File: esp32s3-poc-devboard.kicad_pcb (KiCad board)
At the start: 4 copper layers, 97 parts, among them J1 24VDC, J2 Conn_01x01_Pin, J3 USB_C_Receptacle_USB2.0_14P, J4 USB_C_Receptacle_USB2.0_14P, J5 Screw_Terminal_01x06, J6 Conn_Coaxial, J7 Conn_01x16_Pin, J8 Screw_Terminal_01x04, Q3 MMDT5551, SW1 SW_Push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

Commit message: add 24V symbol and netclass
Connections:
- net Net-(J1-Pin_2) renamed +24V
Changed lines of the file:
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@@
 	(net 3 "+5V")
 	(net 4 "Net-(JP2-A)")
-	(net 5 "Net-(J1-Pin_2)")
+	(net 5 "+24V")
 	(net 6 "Net-(U4-BOOT)")
 	(net 7 "Net-(D3-K)")
@@
 			(layers "*.Cu" "*.Mask")
 			(remove_unused_layers no)
-			(net 5 "Net-(J1-Pin_2)")
+			(net 5 "+24V")
 			(pinfunction "Pin_2")
 			(pintype "passive")
@@
 			(size 1.55 0.6)
 			(layers "F.Cu" "F.Mask" "F.Paste")
-			(net 5 "Net-(J1-Pin_2)")
+			(net 5 "+24V")
 			(pinfunction "VIN")
 			(pintype "power_in")
@@
 			(layers "F.Cu" "F.Mask" "F.Paste")
 			(roundrect_rratio 0.25)
-			(net 5 "Net-(J1-Pin_2)")
+			(net 5 "+24V")
 			(pintype "passive")
 		)

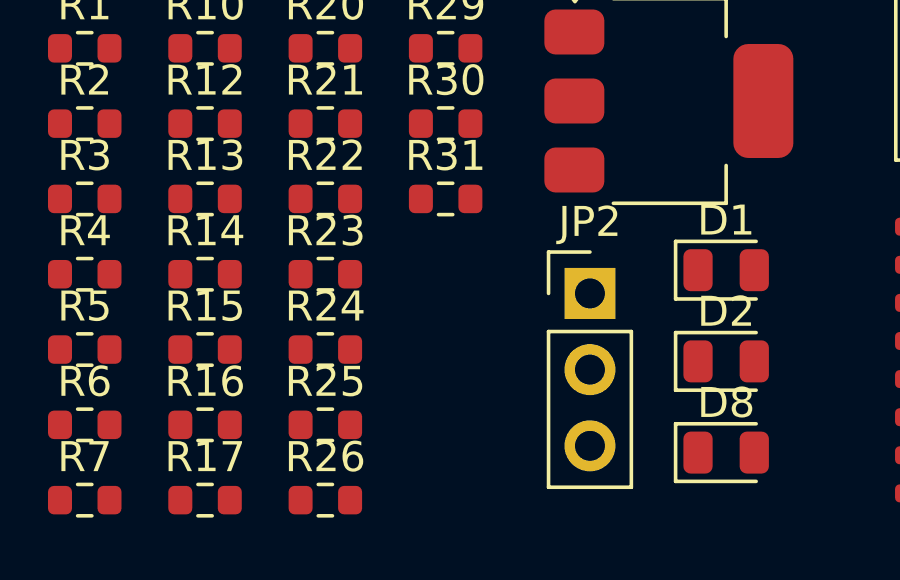
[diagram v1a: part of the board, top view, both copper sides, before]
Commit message: add missing R11 footprint
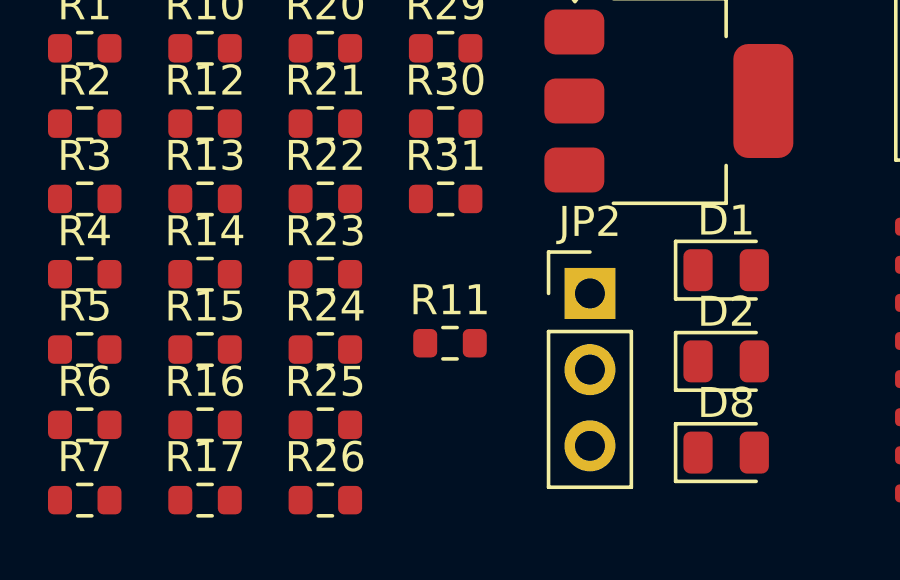
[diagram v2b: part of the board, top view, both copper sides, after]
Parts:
- added R11: R, Resistor_SMD:R_0603_1608Metric, F.Cu at (65.3, 179.5)
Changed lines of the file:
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@@
+		)
+	)
+	(footprint "Resistor_SMD:R_0603_1608Metric"
+		(layer "F.Cu")
+		(at 65.325 179.5)
+		(descr "Resistor SMD 0603 (1608 Metric), square (rectangular) end terminal, IPC-7351 nominal, (Body size source: IPC-SM-782 page 72, https://www.pcb-3d.com/wordpress/wp-content/uploads/ipc-sm-782a_amendment_1_and_2.pdf), generated with kicad-footprint-generator")
+		(tags "resistor")
+		(property "Reference" "R11"
+			(at 0 -1.43 0)
+			(layer "F.SilkS")
+			(effects
+				(font
+					(size 1 1)
+					(thickness 0.15)
+				)
+			)
+		)
+		(property "Value" "R"
+			(at 0 1.43 0)
+			(layer "F.Fab")
+			(effects
+				(font
+					(size 1 1)
+					(thickness 0.15)
+				)
+			)
+		)
+		(property "Datasheet" "~"
+			(at 0 0 0)
+			(layer "F.Fab")
+			(hide yes)
+			(effects
+				(font
+					(size 1.27 1.27)
+					(thickness 0.15)
+				)
+			)
+		)
+		(property "Description" "Resistor"
+			(at 0 0 0)
+			(layer "F.Fab")
+			(hide yes)
+			(effects
+				(font
+					(size 1.27 1.27)
+					(thickness 0.15)
+				)
+			)
+		)
+		(property "JLCPCB Part Number" ""
+			(at 0 0 0)
+			(unlocked yes)
+			(layer "F.Fab")
+			(hide yes)
+			(effects
+				(font
+					(size 1 1)
+					(thickness 0.15)
+				)
+			)
+		)
+		(property "Manufacturer" ""
+			(at 0 0 0)
+			(unlocked yes)
+			(layer "F.Fab")
+			(hide yes)
+			(effects
+				(font
+					(size 1 1)
+					(thickness 0.15)
+				)
+			)
+		)
+		(property "Manufacturer Part Number" ""
+			(at 0 0 0)
+			(unlocked yes)
+			(layer "F.Fab")
+			(hide yes)
+			(effects
+				(font
+					(size 1 1)
+					(thickness 0.15)
+				)
+			)
+		)
+		(property "Basic" ""
+			(at 0 0 0)
+			(unlocked yes)
+			(layer "F.Fab")
+			(hide yes)
+			(effects
+				(font
+					(size 1 1)
+					(thickness 0.15)
+				)
+			)
+		)
+		(property ki_fp_filters "R_*")
+		(sheetname "/")
+		(sheetfile "esp32s3-poc-devboard.kicad_sch")
+		(attr smd dnp)
+		(fp_line
+			(start -0.237258 -0.5225)
+			(end 0.237258 -0.5225)
+			(stroke
+				(width 0.12)
+				(type solid)
+			)
+			(layer "F.SilkS")
+		)
+		(fp_line
+			(start -0.237258 0.5225)
+			(end 0.237258 0.5225)
+			(stroke
+				(width 0.12)
+				(type solid)
+			)
+			(layer "F.SilkS")
+		)
+		(fp_line
+			(start -1.48 -0.73)
+			(end 1.48 -0.73)
+			(stroke
+				(width 0.05)
+				(type solid)
+			)
+			(layer "F.CrtYd")
+		)
+		(fp_line
+			(start -1.48 0.73)
+			(end -1.48 -0.73)
+			(stroke
+				(width 0.05)
+				(type solid)
+			)
+			(layer "F.CrtYd")
+		)
+		(fp_line
+			(start 1.48 -0.73)
+			(end 1.48 0.73)
+			(stroke
+				(width 0.05)
+				(type solid)
+			)
+			(layer "F.CrtYd")
+		)
+		(fp_line
+			(start 1.48 0.73)
+			(end -1.48 0.73)
+			(stroke
+				(width 0.05)
+				(type solid)
+			)
+			(layer "F.CrtYd")
+		)
+		(fp_line
+			(start -0.8 -0.4125)
+			(end 0.8 -0.4125)
+			(stroke
+				(width 0.1)
+				(type solid)
+			)
+			(layer "F.Fab")
+		)
+		(fp_line
+			(start -0.8 0.4125)
+			(end -0.8 -0.4125)
+			(stroke
+				(width 0.1)
+				(type solid)
+			)
+			(layer "F.Fab")
+		)
+		(fp_line
+			(start 0.8 -0.4125)
+			(end 0.8 0.4125)
+			(stroke
+				(width 0.1)
+				(type solid)
+			)
+			(layer "F.Fab")
+		)
+		(fp_line
+			(start 0.8 0.4125)
+			(end -0.8 0.4125)
+			(stroke
+				(width 0.1)
+				(type solid)
+			)
+			(layer "F.Fab")
+		)
+		(fp_text user "${REFERENCE}"
+			(at 0 0 0)
+			(layer "F.Fab")
+			(effects
+				(font
+					(size 0.4 0.4)
+					(thickness 0.06)
+				)
+			)
+		)
+		(pad "1" smd roundrect
+			(at -0.825 0)
+			(size 0.8 0.95)
+			(layers "F.Cu" "F.Mask" "F.Paste")
+			(roundrect_rratio 0.25)
+			(net 16 "/XTAL_32K_P")
+			(pintype "passive")
+		)
+		(pad "2" smd roundrect
+			(at 0.825 0)
+			(size 0.8 0.95)
+			(layers "F.Cu" "F.Mask" "F.Paste")
+			(roundrect_rratio 0.25)
+			(net 17 "/XTAL_32K_N")
+			(pintype "passive")
+		)
+		(embedded_fonts no)
+		(model "${KICAD9_3DMODEL_DIR}/Resistor_SMD.3dshapes/R_0603_1608Metric.step"
+			(offset
+				(xyz 0 0 0)
+			)
+			(scale
+				(xyz 1 1 1)
+			)
+			(rotate
+				(xyz 0 0 0)
+			)
 		)
 	)

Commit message: add net classes colors
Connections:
- net Net-(C23-Pad2) renamed /XTAL_PL
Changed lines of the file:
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@@
 	(net 12 "CHIP_PU")
 	(net 13 "Net-(U5-VBUS)")
-	(net 14 "Net-(C23-Pad2)")
+	(net 14 "/XTAL_PL")
 	(net 15 "/XTAL_N")
 	(net 16 "/XTAL_32K_P")
@@
 			(layers "F.Cu" "F.Mask" "F.Paste")
 			(roundrect_rratio 0.25)
-			(net 14 "Net-(C23-Pad2)")
+			(net 14 "/XTAL_PL")
 			(pinfunction "2")
 			(pintype "passive")
@@
 			(layers "F.Cu" "F.Mask" "F.Paste")
 			(roundrect_rratio 0.25)
-			(net 14 "Net-(C23-Pad2)")
+			(net 14 "/XTAL_PL")
 			(pintype "passive")
 		)
@@
 			(layers "F.Cu" "F.Mask" "F.Paste")
 			(roundrect_rratio 0.25)
-			(net 14 "Net-(C23-Pad2)")
+			(net 14 "/XTAL_PL")
 			(pinfunction "1")
 			(pintype "passive")

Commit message: initial rough pcb placement
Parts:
- moved R2 168.8 mm to (191.2, 75.0)
- moved R3 167.8 mm to (188.2, 75.0)
- moved C3 167.5 mm to (199.9, 83.8), turned to 90 degrees
- moved R7 166.1 mm to (166.2, 63.0)
- moved R6 165.5 mm to (170.0, 65.0)
- moved R4 163.0 mm to (195.0, 97.0)
- moved R1 161.9 mm to (192.9, 87.8)
- moved C4 161.3 mm to (191.9, 84.8), turned to 90 degrees
- moved R5 158.1 mm to (166.0, 69.0), turned to 180 degrees
- moved R25 157.9 mm to (196.5, 100.9), turned to -90 degrees
- moved J1 152.1 mm to (195.8, 54.0), turned to 180 degrees
- moved JP2 150.1 mm to (194.5, 94.0), turned to -90 degrees
- moved SW2 149.5 mm to (167.2, 56.5), turned to 180 degrees
- moved R26 149.1 mm to (184.5, 100.9), turned to 90 degrees
- moved R14 147.5 mm to (179.0, 94.2)
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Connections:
- U6 pad 1: Net-(J3-D--PadA7) -> D-
- U6 pad 3: Net-(J3-D+-PadA6) -> D+
- U6 pad 4: D+ -> Net-(J3-D+-PadA6)
- U6 pad 6: D- -> Net-(J3-D--PadA7)
- U8 pad 12: Net-(J5-Pin_6) -> Net-(J5-Pin_2)
- U8 pad 13: Net-(J5-Pin_5) -> Net-(J5-Pin_3)
- U8 pad 15: Net-(J5-Pin_3) -> Net-(J5-Pin_5)
- U8 pad 16: Net-(J5-Pin_2) -> Net-(J5-Pin_6)

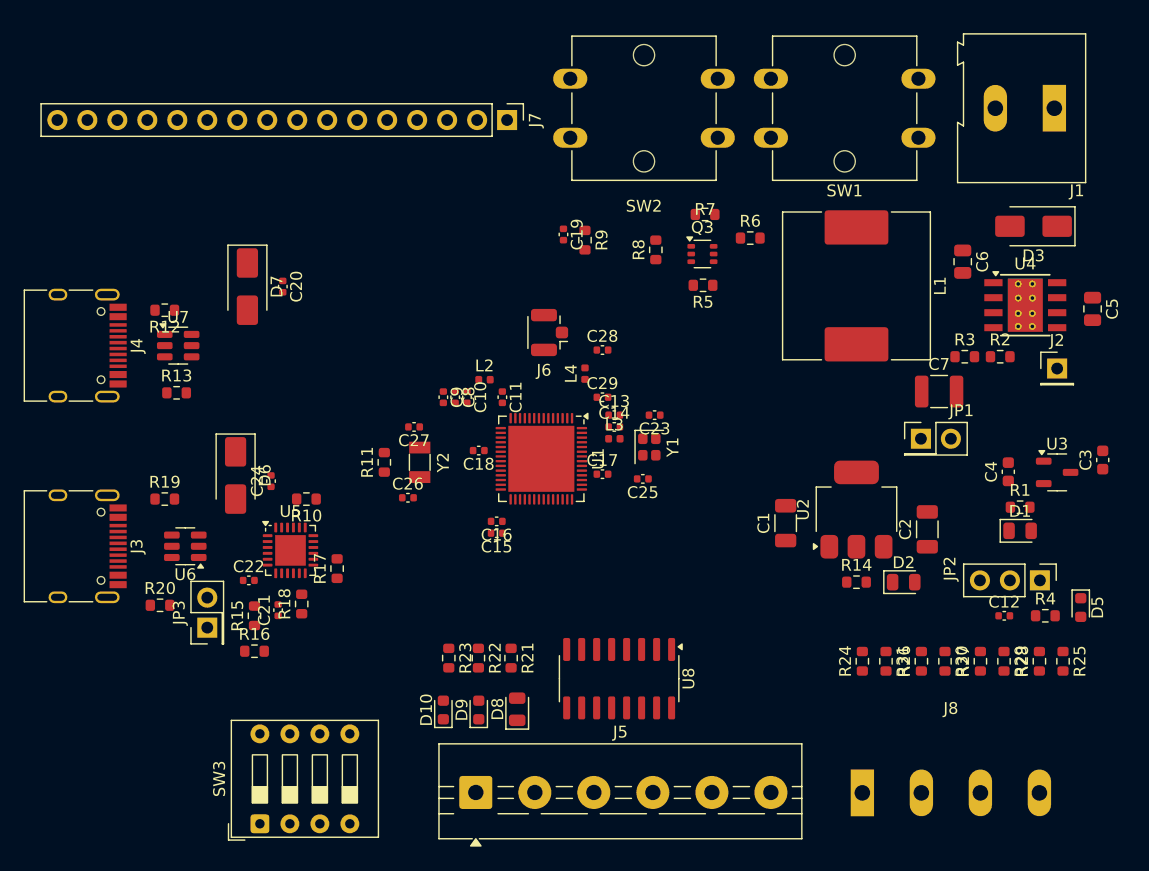
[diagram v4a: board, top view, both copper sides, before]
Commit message: pcb placement refinement
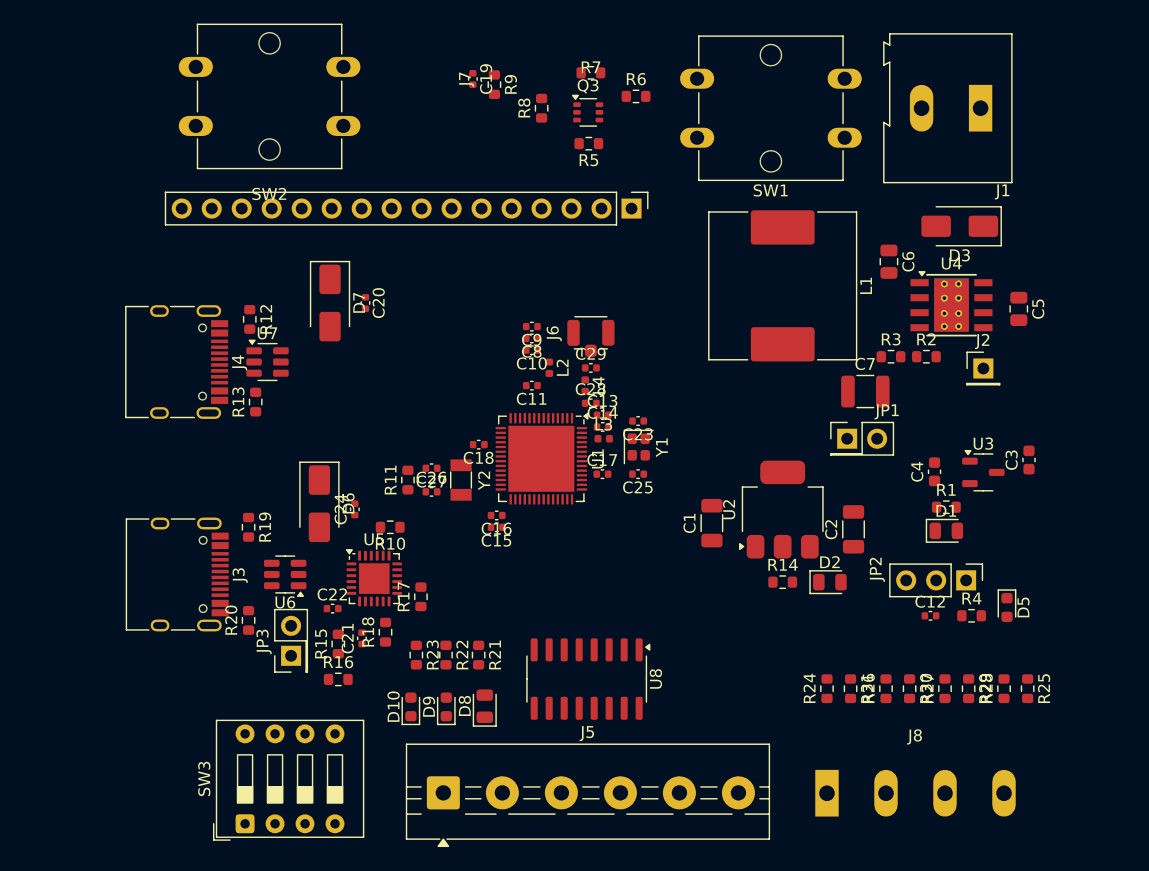
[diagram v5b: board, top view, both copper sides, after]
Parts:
- moved SW2 31.7 mm to (135.5, 55.5)
- moved R5 15.4 mm to (156.3, 57.0)
- moved R6 15.4 mm to (160.3, 53.0)
- moved R7 15.4 mm to (156.5, 51.0)
- moved R8 15.4 mm to (152.3, 54.0)
- moved Q3 15.4 mm to (156.3, 54.4)
- moved R9 15.2 mm to (148.3, 52.0)
- moved C19 15.2 mm to (146.5, 51.5)
- moved J7 12.9 mm to (159.9, 62.5)
- moved C9 9.59 mm to (151.5, 72.5), turned to 180 degrees
- moved J3 8.97 mm to (121.0, 93.5)
- moved U6 8.79 mm to (130.6, 93.5)
- moved J4 8.71 mm to (121.0, 75.5)
- moved C8 8.19 mm to (151.5, 73.5), turned to 180 degrees
- moved U7 7.69 mm to (129.1, 75.5)
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
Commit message: refine usb diode placement
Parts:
- moved C20 4.89 mm to (134.0, 74.0), turned to 180 degrees
- moved C24 4.05 mm to (134.5, 91.5), turned to 180 degrees
- moved D7 2.15 mm to (132.5, 71.5), turned to 180 degrees
- moved D6 1.50 mm to (133.5, 89.0), turned to 180 degrees
- moved J7 1.00 mm to (159.9, 63.5)
- moved SW2 1.00 mm to (135.5, 56.5)

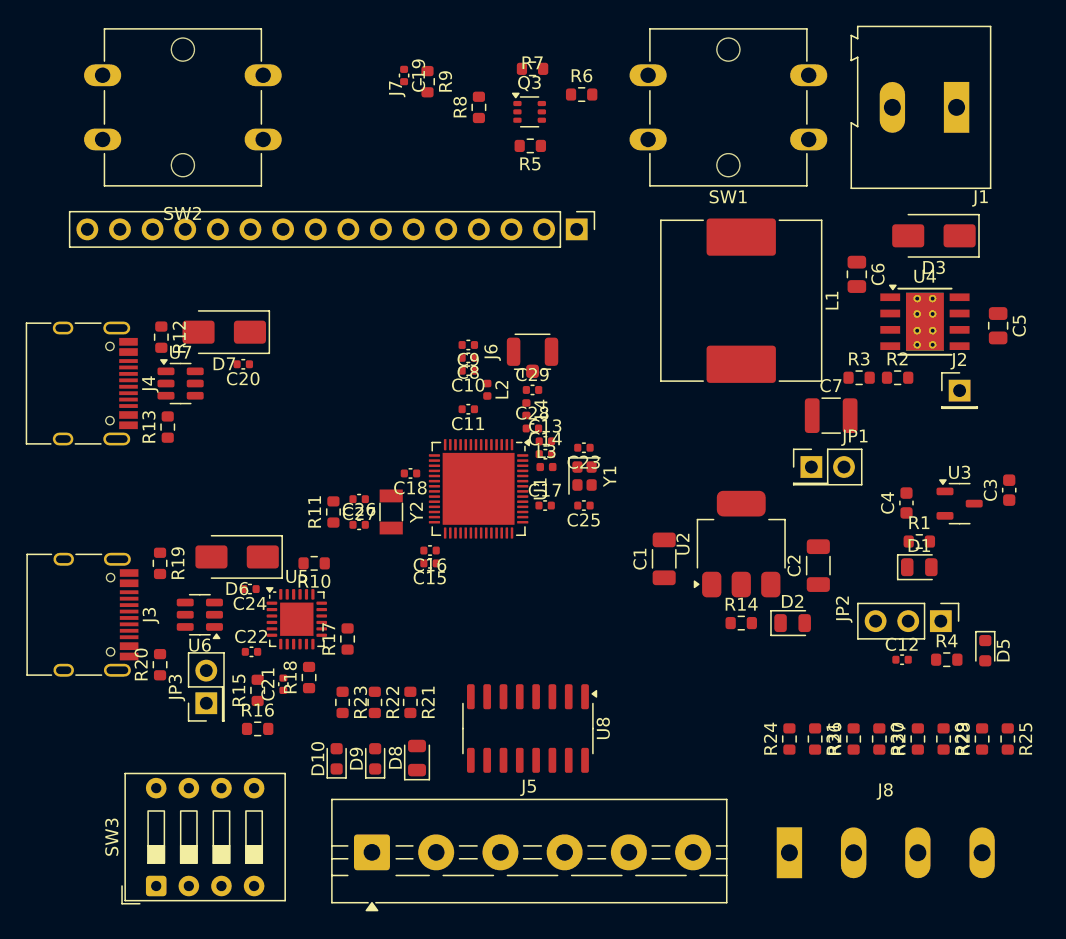
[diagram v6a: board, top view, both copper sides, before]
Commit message: reduce component spread
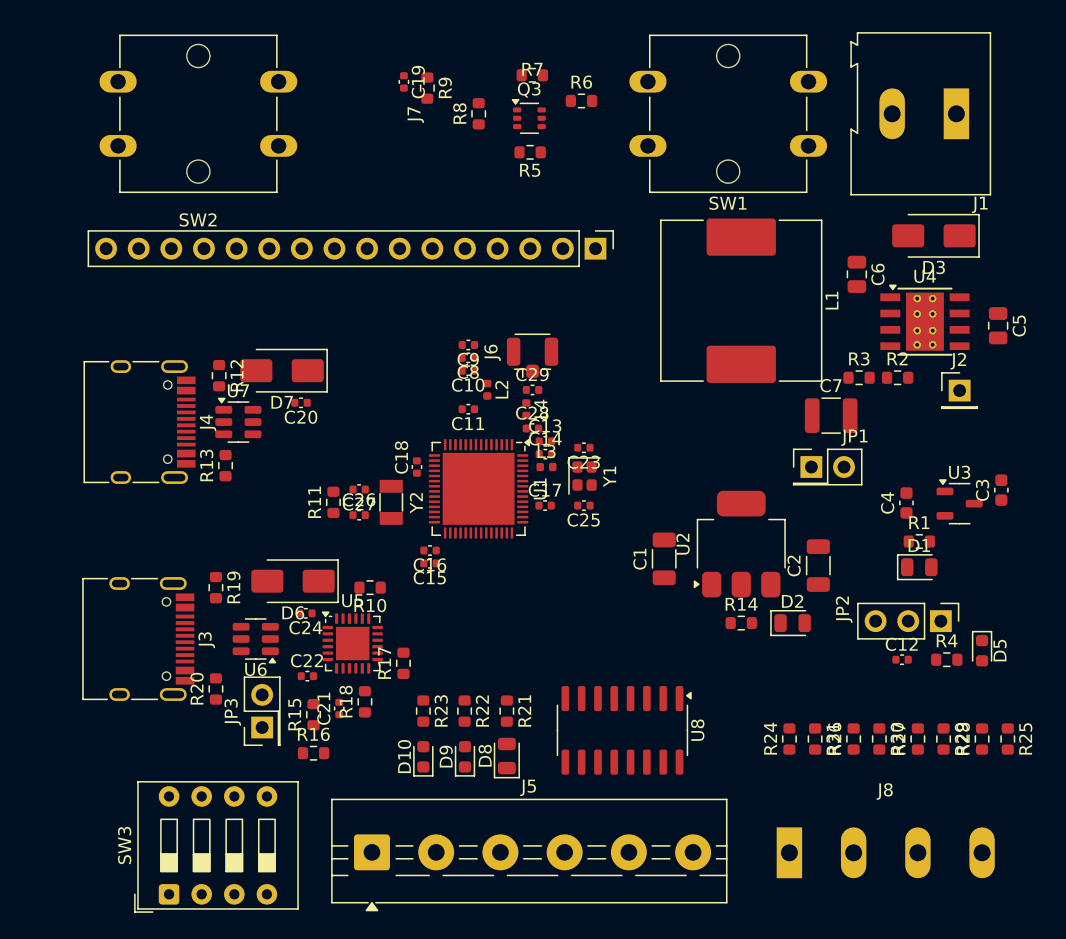
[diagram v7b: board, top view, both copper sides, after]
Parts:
- moved R21 7.54 mm to (154.5, 101.0)
- moved U8 7.36 mm to (163.5, 102.5)
- moved R22 7.03 mm to (151.2, 101.0)
- moved D8 6.99 mm to (154.5, 104.5)
- moved D9 6.99 mm to (151.2, 104.6)
- moved D10 6.75 mm to (148.0, 104.6)
- moved R23 6.33 mm to (148.0, 101.0)
- moved C20 5.41 mm to (138.5, 77.0)
- moved D7 5.41 mm to (137.0, 74.5)
- moved J4 5.41 mm to (125.5, 78.5)
- moved R12 5.41 mm to (132.1, 74.9)
- moved R13 5.41 mm to (132.6, 81.9)
- moved U7 5.41 mm to (133.6, 78.5)
- moved J3 4.74 mm to (125.4, 95.4)
- moved C21 4.74 mm to (141.4, 100.8)
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
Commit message: finish initial component placement
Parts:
- moved C1 12.4 mm to (178.4, 93.2), turned to -90 degrees
- moved R6 11.6 mm to (149.4, 57.7), turned to 90 degrees
- moved C2 11.4 mm to (167.9, 93.3)
- moved R7 10.2 mm to (152.5, 60.9), turned to 180 degrees
- moved R9 9.65 mm to (140.5, 58.2)
- moved D2 8.31 mm to (170.9, 88.2), turned to 180 degrees
- moved C3 7.66 mm to (188.5, 90.0), turned to 180 degrees
- moved C19 6.55 mm to (140.5, 54.7), turned to 90 degrees
- moved U2 6.37 mm to (173.2, 94.3), turned to -90 degrees
- moved R14 6.34 mm to (174.9, 88.2), turned to 180 degrees
- moved C26 6.11 mm to (148.4, 88.6)
- moved R11 5.51 mm to (146.4, 85.8)
- moved C27 5.44 mm to (148.4, 83.1)
- moved Q3 4.85 mm to (152.4, 57.9), turned to 180 degrees
- moved JP1 4.72 mm to (173.5, 82.2), turned to -90 degrees
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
